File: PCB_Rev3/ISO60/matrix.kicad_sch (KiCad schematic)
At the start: 124 parts

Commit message: modify routing
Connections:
- net col_10: now also S59.2; no longer S60.2
- net col_11: now also S60.2; no longer S61.2
- net col_12: now also S41.2, S61.2
- net col_13: no longer S41.2
- net col_9: no longer S59.2
- net row_1: no longer D28.1 (K)
- net row_2: now also D28.1 (K)
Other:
- moved on the sheet: D28, D41, D59, D60, D61, S28, S41, S59, S60, S61

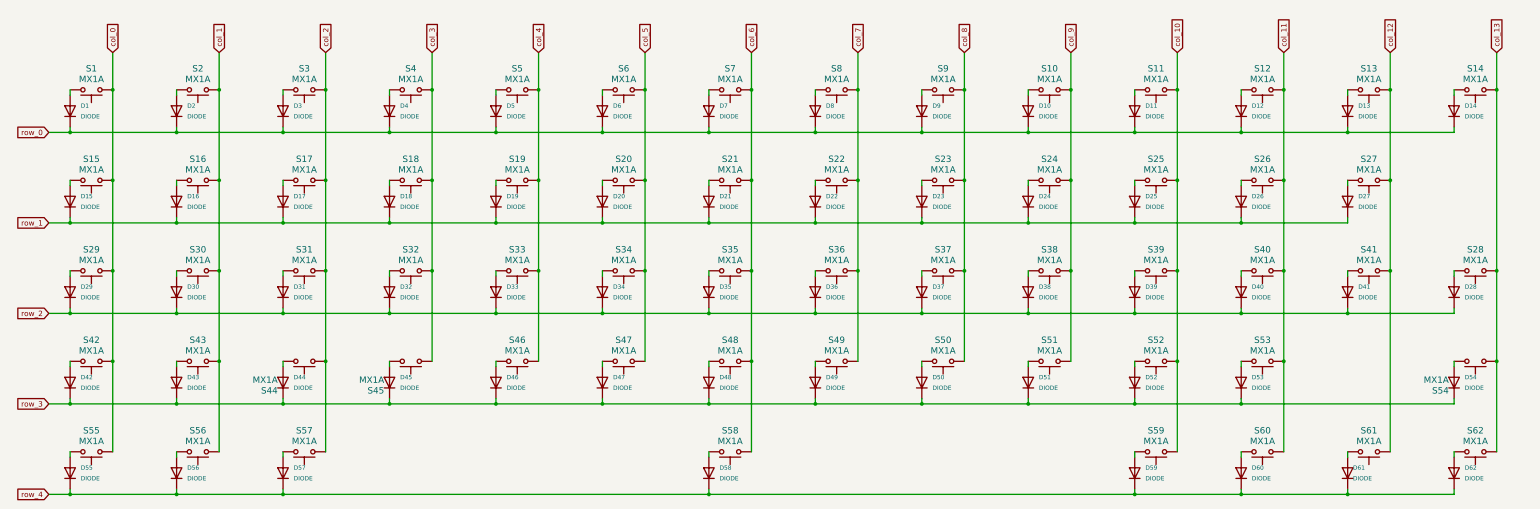
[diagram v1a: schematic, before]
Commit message: Add RGB Lighting for PCB Rev3
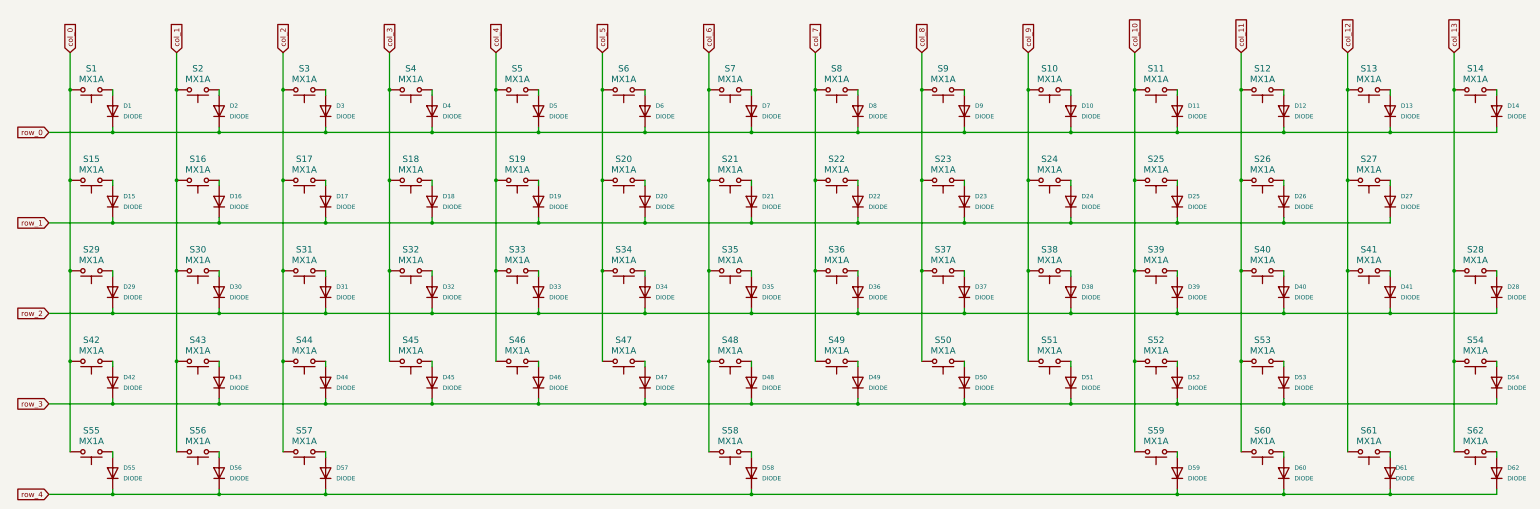
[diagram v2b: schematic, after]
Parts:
- D1, D10, D11, D12, D13, D14, D15, D16, D17, D18, D19, D2, D20, D21, D22, D23, D24, D25, D26, D27, D28, D29, D3, D30, D31, D32, D33, D34, D35, D36, D37, D38, D39, D4, D40, D41, D42, D43, D44, D45, D46, D47, D48, D49, D5, D50, D51, D52, D53, D54, D55, D56, D57, D58, D59, D6, D60, D61, D62, D7, D8, D9: footprint Diode_SMD:D_SOD-123 -> Diode_SMD:D_SOD-323
- S1, S10, S11, S12, S13, S16, S17, S18, S19, S2, S20, S21, S22, S23, S24, S25, S26, S27, S3, S30, S31, S32, S33, S34, S35, S36, S37, S38, S39, S4, S40, S41, S43, S44, S45, S46, S47, S48, S49, S5, S50, S51, S52, S53, S6, S7, S8, S9: footprint PCM_Switch_Keyboard_Hotswap_Kailh:SW_Hotswap_Kailh_MX_1.00u -> PCM_Switch_Keyboard_Hotswap_Kailh:SW_Hotswap_Kailh_MX_Plated_1.00u
- S14: footprint PCM_Switch_Keyboard_Hotswap_Kailh:SW_Hotswap_Kailh_MX_2.00u -> PCM_Switch_Keyboard_Hotswap_Kailh:SW_Hotswap_Kailh_MX_Plated_2.00u
- S15: footprint PCM_Switch_Keyboard_Hotswap_Kailh:SW_Hotswap_Kailh_MX_1.50u -> PCM_Switch_Keyboard_Hotswap_Kailh:SW_Hotswap_Kailh_MX_Plated_1.50u
- S28: footprint PCM_Switch_Keyboard_Hotswap_Kailh:SW_Hotswap_Kailh_MX_ISOEnter -> PCM_Switch_Keyboard_Hotswap_Kailh:SW_Hotswap_Kailh_MX_Plated_ISOEnter
- S29: footprint PCM_Switch_Keyboard_Hotswap_Kailh:SW_Hotswap_Kailh_MX_1.75u -> PCM_Switch_Keyboard_Hotswap_Kailh:SW_Hotswap_Kailh_MX_Plated_1.75u
- S42, S55, S56, S57, S59, S60, S61, S62: footprint PCM_Switch_Keyboard_Hotswap_Kailh:SW_Hotswap_Kailh_MX_1.25u -> PCM_Switch_Keyboard_Hotswap_Kailh:SW_Hotswap_Kailh_MX_Plated_1.25u
- S54: footprint PCM_Switch_Keyboard_Hotswap_Kailh:SW_Hotswap_Kailh_MX_2.75u -> PCM_Switch_Keyboard_Hotswap_Kailh:SW_Hotswap_Kailh_MX_Plated_2.75u
- S58: footprint PCM_Switch_Keyboard_Hotswap_Kailh:SW_Hotswap_Kailh_MX_6.25u -> PCM_Switch_Keyboard_Hotswap_Kailh:SW_Hotswap_Kailh_MX_Plated_6.25u
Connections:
- net col_0: now also S1.1, S15.1, S29.1, S42.1, S55.1; no longer S1.2, S15.2, S29.2, S42.2, S55.2
- net col_1: now also S16.1, S2.1, S30.1, S43.1, S56.1; no longer S16.2, S2.2, S30.2, S43.2, S56.2
- net col_10: now also S11.1, S25.1, S39.1, S52.1, S59.1; no longer S11.2, S25.2, S39.2, S52.2, S59.2
- net col_11: now also S12.1, S26.1, S40.1, S53.1, S60.1; no longer S12.2, S26.2, S40.2, S53.2, S60.2
- net col_12: now also S13.1, S27.1, S41.1, S61.1; no longer S13.2, S27.2, S41.2, S61.2
- net col_13: now also S14.1, S28.1, S54.1, S62.1; no longer S14.2, S28.2, S54.2, S62.2
- net col_2: now also S17.1, S3.1, S31.1, S44.1, S57.1; no longer S17.2, S3.2, S31.2, S44.2, S57.2
- net col_3: now also S18.1, S32.1, S4.1, S45.1; no longer S18.2, S32.2, S4.2, S45.2
- net col_4: now also S19.1, S33.1, S46.1, S5.1; no longer S19.2, S33.2, S46.2, S5.2
- net col_5: now also S20.1, S34.1, S47.1, S6.1; no longer S20.2, S34.2, S47.2, S6.2
- net col_6: now also S21.1, S35.1, S48.1, S58.1, S7.1; no longer S21.2, S35.2, S48.2, S58.2, S7.2
- net col_7: now also S22.1, S36.1, S49.1, S8.1; no longer S22.2, S36.2, S49.2, S8.2
- net col_8: now also S23.1, S37.1, S50.1, S9.1; no longer S23.2, S37.2, S50.2, S9.2
- net col_9: now also S10.1, S24.1, S38.1, S51.1; no longer S10.2, S24.2, S38.2, S51.2
- net at D33.2 (A): now also S33.2; no longer S33.1
- net at D9.2 (A): now also S9.2; no longer S9.1
- net at D62.2 (A): now also S62.2; no longer S62.1
- net at D14.2 (A): now also S14.2; no longer S14.1
- net at D46.2 (A): now also S46.2; no longer S46.1
- net at D56.2 (A): now also S56.2; no longer S56.1
- net at D2.2 (A): now also S2.2; no longer S2.1
- net at D43.2 (A): now also S43.2; no longer S43.1
- net at D7.2 (A): now also S7.2; no longer S7.1
- net at D42.2 (A): now also S42.2; no longer S42.1
- net at D16.2 (A): now also S16.2; no longer S16.1
- net at D60.2 (A): now also S60.2; no longer S60.1
- net at D58.2 (A): now also S58.2; no longer S58.1
- net at D40.2 (A): now also S40.2; no longer S40.1
- net at D51.2 (A): now also S51.2; no longer S51.1
- net at D35.2 (A): now also S35.2; no longer S35.1
- net at D44.2 (A): now also S44.2; no longer S44.1
- net at D28.2 (A): now also S28.2; no longer S28.1
- net at D47.2 (A): now also S47.2; no longer S47.1
- net at D13.2 (A): now also S13.2; no longer S13.1
- net at D23.2 (A): now also S23.2; no longer S23.1
- net at D18.2 (A): now also S18.2; no longer S18.1
- net at D3.2 (A): now also S3.2; no longer S3.1
- net at D24.2 (A): now also S24.2; no longer S24.1
- net at D45.2 (A): now also S45.2; no longer S45.1
- net at D1.2 (A): now also S1.2; no longer S1.1
- net at D30.2 (A): now also S30.2; no longer S30.1
- net at D11.2 (A): now also S11.2; no longer S11.1
- net at D41.2 (A): now also S41.2; no longer S41.1
- net at D4.2 (A): now also S4.2; no longer S4.1
- net at D57.2 (A): now also S57.2; no longer S57.1
- net at D32.2 (A): now also S32.2; no longer S32.1
- net at D61.2 (A): now also S61.2; no longer S61.1
- net at D25.2 (A): now also S25.2; no longer S25.1
- net at D15.2 (A): now also S15.2; no longer S15.1
- net at D39.2 (A): now also S39.2; no longer S39.1
- net at D8.2 (A): now also S8.2; no longer S8.1
- net at D49.2 (A): now also S49.2; no longer S49.1
- net at D52.2 (A): now also S52.2; no longer S52.1
- net at D19.2 (A): now also S19.2; no longer S19.1
- net at D50.2 (A): now also S50.2; no longer S50.1
- net at D59.2 (A): now also S59.2; no longer S59.1
- net at D21.2 (A): now also S21.2; no longer S21.1
- net at D22.2 (A): now also S22.2; no longer S22.1
- net at D37.2 (A): now also S37.2; no longer S37.1
- net at D48.2 (A): now also S48.2; no longer S48.1
- net at D53.2 (A): now also S53.2; no longer S53.1
- net at D27.2 (A): now also S27.2; no longer S27.1
- net at D55.2 (A): now also S55.2; no longer S55.1
- net at D10.2 (A): now also S10.2; no longer S10.1
- net at D31.2 (A): now also S31.2; no longer S31.1
- net at D34.2 (A): now also S34.2; no longer S34.1
- net at D12.2 (A): now also S12.2; no longer S12.1
- net at D29.2 (A): now also S29.2; no longer S29.1
- net at D6.2 (A): now also S6.2; no longer S6.1
- net at D36.2 (A): now also S36.2; no longer S36.1
- net at D5.2 (A): now also S5.2; no longer S5.1
- net at D20.2 (A): now also S20.2; no longer S20.1
- net at D26.2 (A): now also S26.2; no longer S26.1
- net at D17.2 (A): now also S17.2; no longer S17.1
- net at D54.2 (A): now also S54.2; no longer S54.1
- net at D38.2 (A): now also S38.2; no longer S38.1
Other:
- moved on the sheet: D1, D10, D11, D12, D13, D14, D15, D16, D17, D18, D19, D2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
